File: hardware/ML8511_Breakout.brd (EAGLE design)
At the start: 15.2 x 15.2 mm, 10 parts, among them U1 ML8511-UV-SENSOR

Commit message: Small changes to layout.
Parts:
- moved LOGO2 33.1 mm to (-5.08, 3.81)

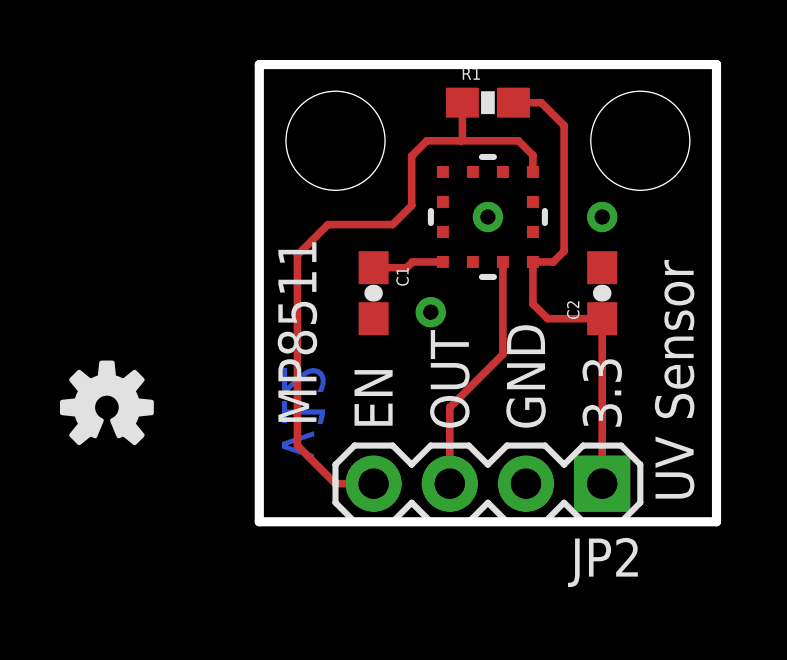
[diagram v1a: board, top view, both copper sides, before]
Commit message: DFM Changes
1.) Modified 3.3V trace so junction is not on IC pad
2.) Added trestrict under IC
3.) Routed GND trace directly away from IC
4.) Modified silk to better incorporate OSHW logo
5.) Version numbers between sch and brd are now consistent at v10
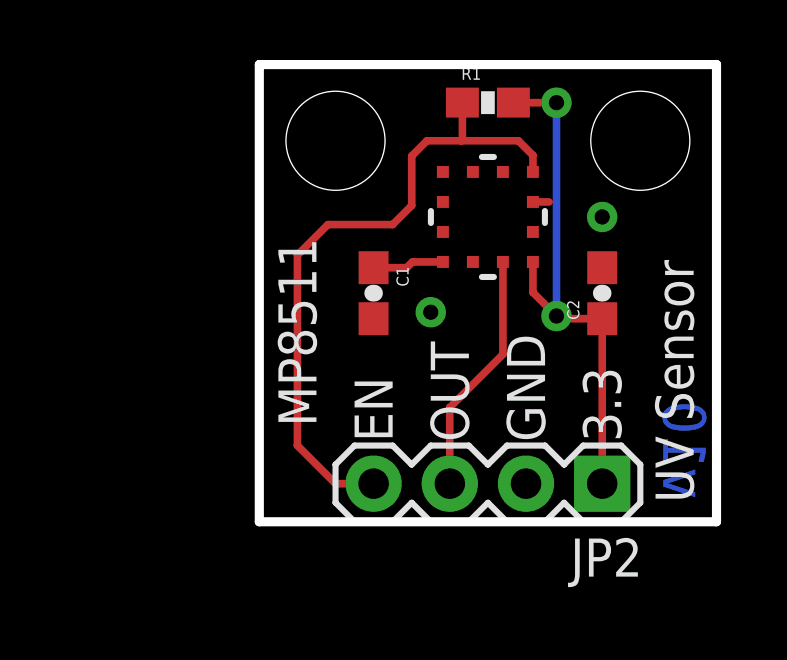
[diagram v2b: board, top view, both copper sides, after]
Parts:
- removed LOGO1: SFE_LOGO_NAME_FLAME.1_INCH, SparkFun-Aesthetics:SFE_LOGO_NAME_FLAME_.1
- added LOGO3: SFE_LOGO_FLAME.1_INCH, SparkFun-Aesthetics:SFE_LOGO_FLAME_.1
- added LOGO4: SFE_LOGO_NAME.1_INCH, SparkFun-Aesthetics:SFE_LOGO_NAME_.1
- moved LOGO2 16.1 mm to (8.64, 12.3), flipped to the bottom
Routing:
- net 3.3V: track 16.8 -> 17.7 mm, vias 0 -> 2
- net GND: track 0.00 -> 0.54 mm, vias 3 -> 2
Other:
- board text added: "v10"
- board text removed: "v12"
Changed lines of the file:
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@@
 <layer number="47" name="Measures" color="7" fill="1" visible="no" active="yes"/>
 <layer number="48" name="Document" color="7" fill="1" visible="no" active="yes"/>
-<layer number="49" name="Reference" color="7" fill="1" visible="yes" active="yes"/>
+<layer number="49" name="Reference" color="7" fill="1" visible="no" active="yes"/>
 <layer number="50" name="dxf" color="7" fill="1" visible="no" active="yes"/>
 <layer number="51" name="tDocu" color="6" fill="1" visible="yes" active="yes"/>
@@
 <wire x1="15.24" y1="0" x2="15.24" y2="15.24" width="0.3048" layer="20"/>
 <wire x1="15.24" y1="15.24" x2="0" y2="15.24" width="0.3048" layer="20"/>
-<text x="0.762" y="2.032" size="1.4224" layer="16" font="vector" ratio="20" rot="MR90">v12</text>
+<text x="13.462" y="0.762" size="1.4224" layer="16" font="vector" ratio="20" rot="MR90">v10</text>
 <text x="15.24" y="-10.16" size="1.778" layer="48" font="vector" ratio="15">N. Seidle</text>
-<text x="12.065" y="3.048" size="1.27" layer="21" font="vector" ratio="15" rot="R90">3.3</text>
+<text x="12.065" y="2.667" size="1.27" layer="21" font="vector" ratio="15" rot="R90">3.3</text>
 <text x="1.905" y="3.175" size="1.27" layer="21" font="vector" ratio="15" rot="SR90">MP8511</text>
-<text x="9.525" y="3.048" size="1.27" layer="21" font="vector" ratio="15" rot="R90">GND</text>
-<text x="6.985" y="3.048" size="1.27" layer="21" font="vector" ratio="15" rot="R90">OUT</text>
-<text x="4.445" y="3.048" size="1.27" layer="21" font="vector" ratio="15" rot="R90">EN</text>
-<text x="10.795" y="3.048" size="1.27" layer="22" font="vector" ratio="15" rot="MR90">3.3V</text>
-<text x="8.255" y="3.048" size="1.27" layer="22" font="vector" ratio="15" rot="MR90">GND</text>
-<text x="5.715" y="3.048" size="1.27" layer="22" font="vector" ratio="15" rot="MR90">OUT</text>
+<text x="9.525" y="2.667" size="1.27" layer="21" font="vector" ratio="15" rot="R90">GND</text>
+<text x="6.985" y="2.667" size="1.27" layer="21" font="vector" ratio="15" rot="R90">OUT</text>
+<text x="4.445" y="2.667" size="1.27" layer="21" font="vector" ratio="15" rot="R90">EN</text>
+<text x="10.795" y="2.667" size="1.27" layer="22" font="vector" ratio="15" rot="MR90">3.3V</text>
+<text x="8.255" y="2.667" size="1.27" layer="22" font="vector" ratio="15" rot="MR90">GND</text>
+<text x="5.715" y="2.667" size="1.27" layer="22" font="vector" ratio="15" rot="MR90">OUT</text>
 <text x="3.175" y="3.048" size="1.27" layer="22" font="vector" ratio="15" rot="MR90">EN</text>
 <text x="14.478" y="0.635" size="1.27" layer="21" font="vector" ratio="15" rot="R90">UV Sensor</text>
+<rectangle x1="6.604" y1="9.271" x2="8.636" y2="11.176" layer="41"/>
+<rectangle x1="9.017" y1="11.049" x2="9.144" y2="11.176" layer="41"/>
+<rectangle x1="9.017" y1="10.16" x2="9.144" y2="10.287" layer="41"/>
+<text x="11.43" y="-10.16" size="1.778" layer="51" ratio="15">N. Seidle</text>
 </plain>
 <attributes>
@@
 <attribute name="PROD_ID" value="RES-00824" x="7.62" y="13.97" size="1.778" layer="27" font="vector" ratio="15" display="off"/>
 </element>
-<element name="LOGO1" library="SparkFun-Aesthetics" package="SFE_LOGO_NAME_FLAME_.1" value="SFE_LOGO_NAME_FLAME.1_INCH" x="13.589" y="7.874" rot="MR0"/>
-<element name="LOGO2" library="SparkFun-Aesthetics" package="OSHW-LOGO-S" value="OSHW-LOGOS" x="-5.08" y="3.81"/>
+<element name="LOGO2" library="SparkFun-Aesthetics" package="OSHW-LOGO-S" value="OSHW-LOGOS" x="8.636" y="12.319" rot="MR0"/>
+<element name="LOGO3" library="SparkFun-Aesthetics" package="SFE_LOGO_FLAME_.1" value="SFE_LOGO_FLAME.1_INCH" x="6.858" y="10.795" rot="MR0"/>
+<element name="LOGO4" library="SparkFun-Aesthetics" package="SFE_LOGO_NAME_.1" value="SFE_LOGO_NAME.1_INCH" x="13.589" y="6.35" rot="MR0"/>
 </elements>
 <signals>
@@
 <via x="11.43" y="10.16" extent="1-16" drill="0.508"/>
 <via x="5.715" y="6.985" extent="1-16" drill="0.508"/>
-<via x="7.62" y="10.16" extent="1-16" drill="0.508"/>
+<wire x1="9.12" y1="10.66" x2="9.66" y2="10.66" width="0.254" layer="1"/>
 </signal>
 <signal name="3.3V">
@@
 <contactref element="C2" pad="1"/>
 <contactref element="JP2" pad="1"/>
-<wire x1="9.12" y1="8.66" x2="9.12" y2="7.263" width="0.254" layer="1"/>
-<wire x1="9.12" y1="7.263" x2="9.613" y2="6.77" width="0.254" layer="1"/>
-<wire x1="11.43" y1="6.77" x2="9.613" y2="6.77" width="0.254" layer="1"/>
 <contactref element="R1" pad="2"/>
-<wire x1="9.12" y1="8.66" x2="9.803" y2="8.66" width="0.254" layer="1"/>
-<wire x1="9.803" y1="8.66" x2="10.16" y2="9.017" width="0.254" layer="1"/>
-<wire x1="10.16" y1="9.017" x2="10.16" y2="13.208" width="0.254" layer="1"/>
-<wire x1="10.16" y1="13.208" x2="9.398" y2="13.97" width="0.254" layer="1"/>
-<wire x1="9.398" y1="13.97" x2="8.47" y2="13.97" width="0.254" layer="1"/>
 <wire x1="11.43" y1="6.77" x2="11.43" y2="1.27" width="0.254" layer="1"/>
+<via x="9.906" y="13.97" extent="1-16" drill="0.508"/>
+<wire x1="9.906" y1="13.97" x2="9.906" y2="6.858" width="0.254" layer="16"/>
+<wire x1="8.47" y1="13.97" x2="9.906" y2="13.97" width="0.254" layer="1"/>
+<via x="9.906" y="6.858" extent="1-16" drill="0.508"/>
+<wire x1="9.12" y1="8.66" x2="9.12" y2="7.644" width="0.254" layer="1"/>
+<wire x1="9.12" y1="7.644" x2="9.906" y2="6.858" width="0.254" layer="1"/>
+<wire x1="11.43" y1="6.77" x2="9.994" y2="6.77" width="0.254" layer="1"/>
+<wire x1="9.994" y1="6.77" x2="9.906" y2="6.858" width="0.254" layer="1"/>
 </signal>
 <signal name="ENABLE">
